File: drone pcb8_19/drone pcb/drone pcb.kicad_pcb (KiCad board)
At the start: 2 copper layers, 50 x 65 mm, 9 parts, among them U1 MS560702BA03-50

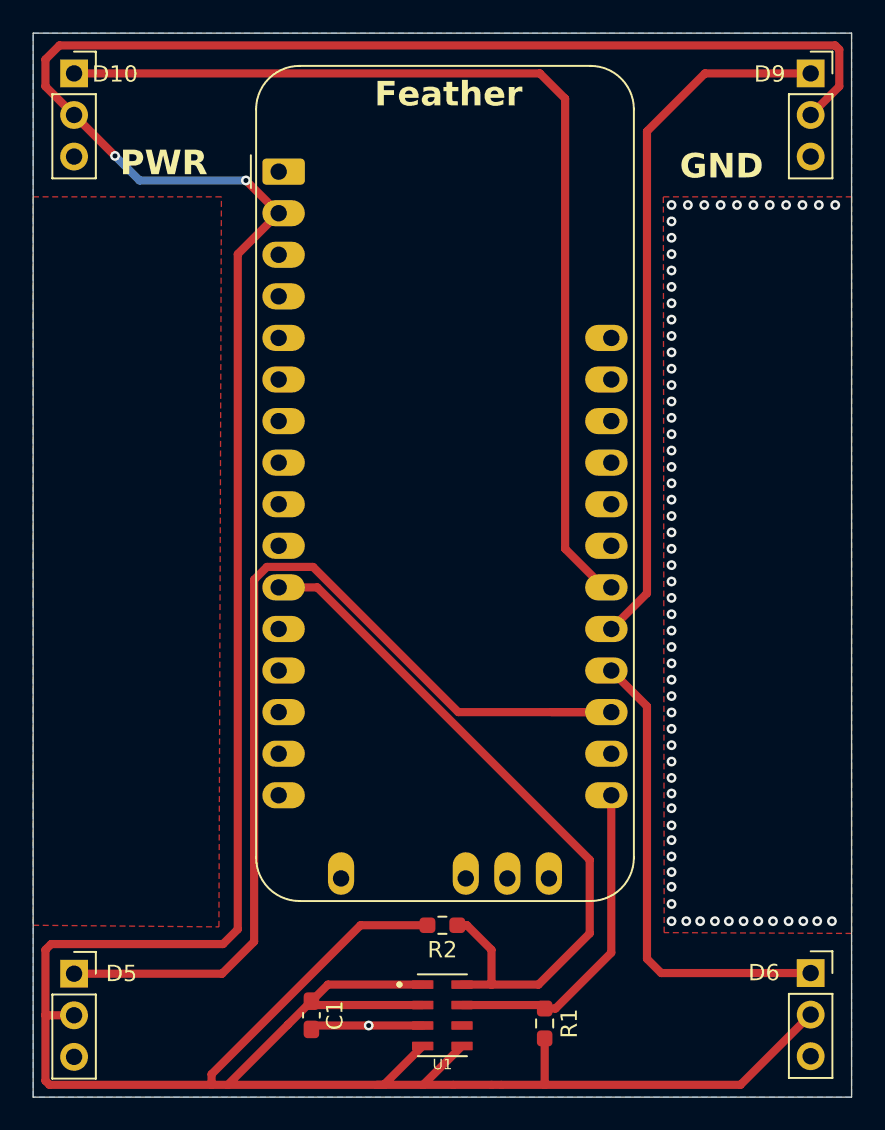
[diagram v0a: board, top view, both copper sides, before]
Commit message: add feather power off battery
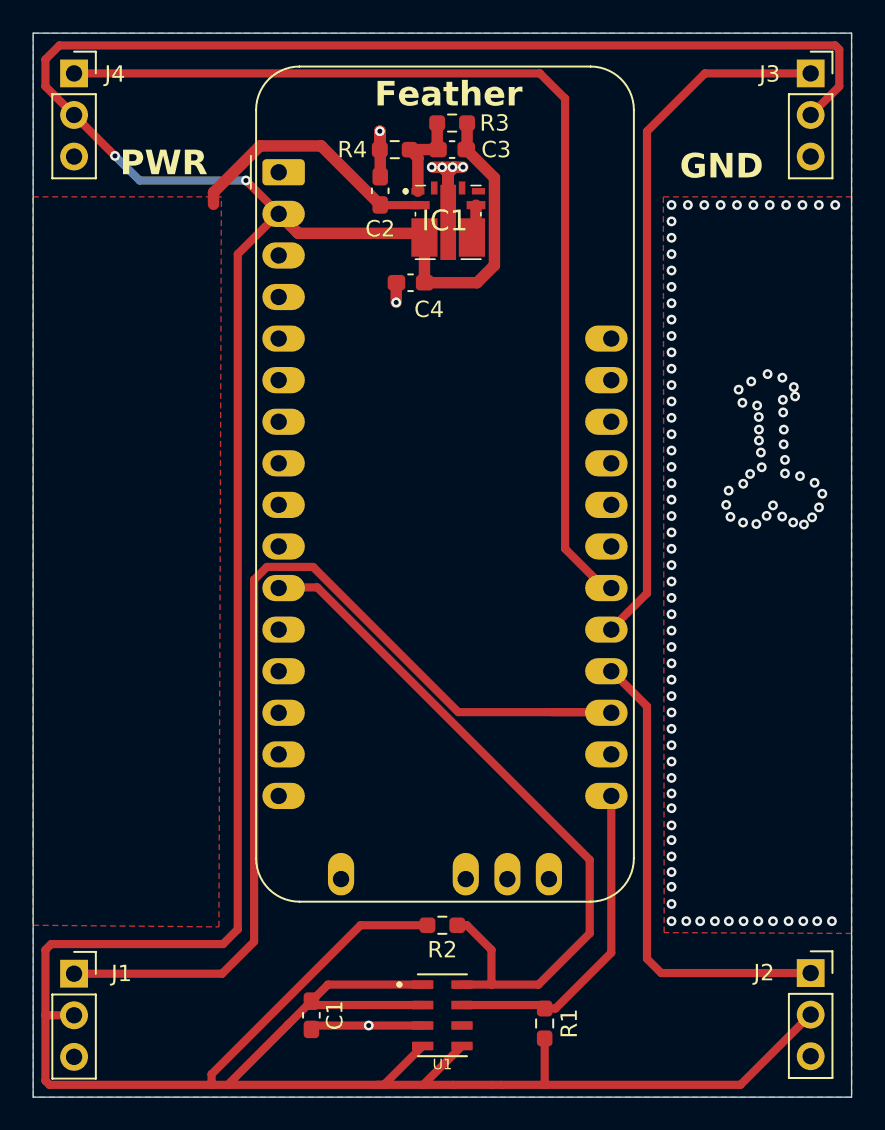
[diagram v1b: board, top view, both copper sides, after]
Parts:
- added C2: 6.8uF, Capacitor_SMD:C_0603_1608Metric_Pad1.08x0.95mm_HandSolder, F.Cu at (81.2, 54.1)
- added C3: 330pF, Capacitor_SMD:C_0603_1608Metric_Pad1.08x0.95mm_HandSolder, F.Cu at (85.6, 51.6)
- added C4: 47uF, Capacitor_SMD:C_0603_1608Metric_Pad1.08x0.95mm_HandSolder, F.Cu at (83.1, 59.7)
- added IC1: TPSM84209RKHT, KiCad:TPSM84209RKHT, F.Cu at (85.4, 56.1)
- added R3: 10kOhm, Resistor_SMD:R_0603_1608Metric_Pad0.98x0.95mm_HandSolder, F.Cu at (85.6, 50.0)
- added R4: 2.2kOhm, Resistor_SMD:R_0603_1608Metric_Pad0.98x0.95mm_HandSolder, F.Cu at (82.1, 51.6)
- renumbered D5 to J1, D6 to J2, D9 to J3, D10 to J4
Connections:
- A1 pad 4: GND -> unconnected-(A1-GND-Pad4)
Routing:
- net +3.3V: track 237.0 -> 263.4 mm
- net +VDC: track 0.00 -> 16.0 mm
- net GND: track 6.90 -> 21.6 mm, vias 67 -> 109
- net Net-(IC1-FB): track 0.00 -> 6.26 mm
- net Net-(IC1-SW_1): track 0.00 -> 2.08 mm
